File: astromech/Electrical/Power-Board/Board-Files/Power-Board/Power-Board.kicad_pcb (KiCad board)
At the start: 2 copper layers, 119.4 x 96.5 mm, 74 parts, among them J1 BAT_IN_SCREW, J10 HEAD_MOT, J2 BAT_IN_HOLE, J5 E_STOP, J6 CTRL_BRD, J7 JETSON, J8 L_DRIVE, J9 R_DRIVE, Q1 Q_NMOS_DSG, Q2 Q_NMOS_DSG, U1 LTC7003, U2 Logic_Level_Converter, U3 12V_REG, U4 LTC7003, U5 5V_REG, U6 3.3V_REG

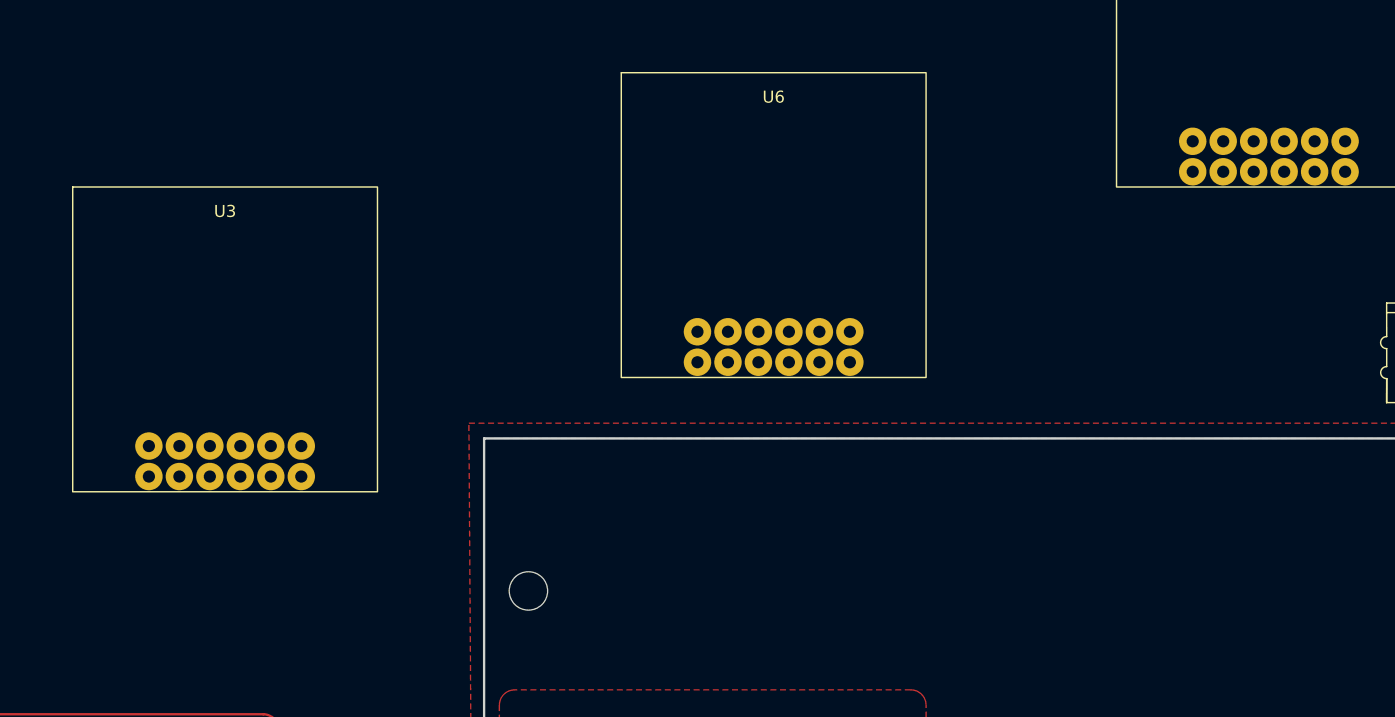
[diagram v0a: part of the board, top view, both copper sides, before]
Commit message: Moved regulator fuses
Moved regulator fuses to voltage input
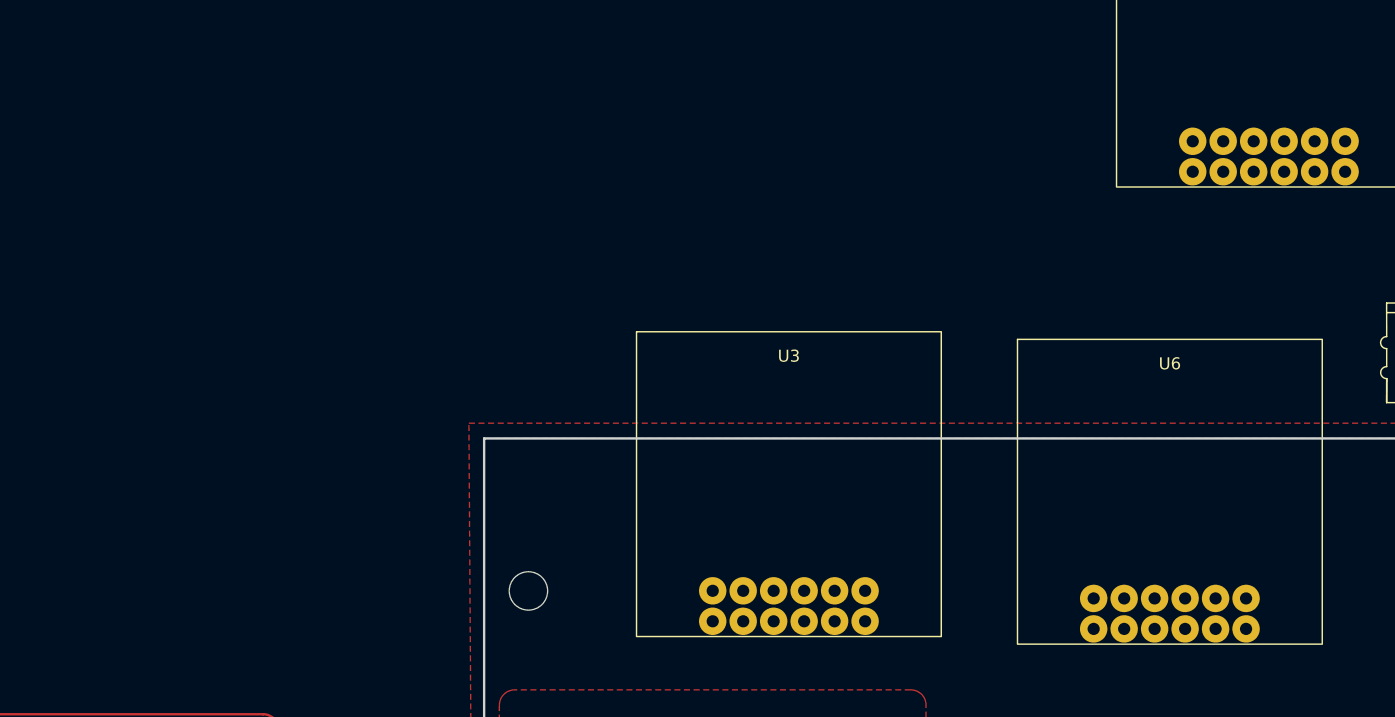
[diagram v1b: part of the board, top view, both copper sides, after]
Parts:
- moved U3 48.5 mm to (101.6, 41.9)
- moved U6 39.8 mm to (133.3, 42.5)
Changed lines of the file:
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@@
   )
   (footprint "astromech-footprints:D36V50Fx" (layer "F.Cu")
-    (at 100.33 20.32)
+    (at 133.35 42.545)
     (property "Sheetfile" "Power-Board.kicad_sch")
     (property "Sheetname" "")
@@
   )
   (footprint "astromech-footprints:D36V50Fx" (layer "F.Cu")
-    (at 54.61 29.845)
-    (property "Sheetfile" "Power-Board.kicad_sch")
-    (property "Sheetname" "")
+    (at 101.6 41.91)
+    (property "Sheetfile" "Power-Board.kicad_sch")
+    (property "Sheetname" "")

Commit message: layout changes
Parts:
- moved SIG-CONV-LV1 389.4 mm to (6.74, 137.1)
- moved SIG-CONV-LV2 382.3 mm to (22.9, 137.4)
- moved C9 245.6 mm to (151.1, 148.0)
- moved 5V4 243.5 mm to (182.2, 123.8)
- moved 5V3 242.2 mm to (170.8, 123.8)
- moved 5V2 241.0 mm to (159.4, 123.8)
- moved SIG-CONV-HV2 240.8 mm to (94.1, 87.6), turned to -90 degrees
- moved 5V1 239.7 mm to (148.0, 123.8)
- moved SIG-CONV-HV1 222.1 mm to (93.9, 108.8), turned to -90 degrees
- moved U3 175.3 mm to (270.5, 88.9), turned to 180 degrees
- moved 3.3V4 148.0 mm to (184.8, 68.6), turned to 90 degrees
- moved U5 133.1 mm to (244.5, 88.9), turned to 180 degrees
- moved 3.3V3 132.8 mm to (184.8, 80.0), turned to 90 degrees
- moved 12V4 127.8 mm to (136.5, 123.8)
- moved 12V3 126.5 mm to (125.1, 123.8)
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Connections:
- F2 pad 1: 12V_REG -> +BATT
- F3 pad 1: 5V_REG -> +BATT
- F4 pad 1: Net-(F4-Pad1) -> Net-(U6-Pad3)
- F4 pad 2: 3.3V_REG -> +BATT
- U3 pad 1: Net-(F2-Pad2) -> 12V_REG
- U3 pad 3: +BATT -> Net-(F2-Pad2)
- U5 pad 1: Net-(F3-Pad2) -> 5V_REG
- U5 pad 3: +BATT -> Net-(F3-Pad2)
- U6 pad 1: Net-(F4-Pad1) -> 3.3V_REG
- U6 pad 3: +BATT -> Net-(U6-Pad3)
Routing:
- removed copper zone on F.Cu, net Net-(F1-Pad1)
- removed copper zone on F.Cu, net POW+

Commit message: First fully routed board version
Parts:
- C1, C10, C2, C3, C4, C5, C6, C7, C8, C9, D1, D2, R1, R10, R11, R12, R13, R14, R2, R3, R4, R5, R6, R7, R8, R9, TP1, TP2, U1, U4: moved to B.Cu
- moved U2 186.1 mm to (159.4, 62.9)
- moved SIG-CONV-LV2 145.6 mm to (138.4, 48.9), turned to 180 degrees
- moved SIG-CONV-LV1 145.5 mm to (122.5, 48.9), turned to 180 degrees
- moved U3 112.3 mm to (158.8, 99.7)
- moved U5 112.3 mm to (132.7, 99.7)
- moved U6 111.6 mm to (106.7, 99.7)
- moved F2 111.1 mm to (158.8, 83.2), turned to 0 degrees
- moved 3.3V4 110.2 mm to (87.0, 119.4), turned to -90 degrees
- moved F3 106.2 mm to (137.8, 83.8), turned to 180 degrees
- moved F4 105.5 mm to (111.8, 83.8), turned to 0 degrees
- moved SIG-CONV-HV1 103.1 mm to (177.8, 48.9), turned to 180 degrees
- moved 3.3V3 101.9 mm to (87.0, 108.6), turned to -90 degrees
- moved D1 100.2 mm to (144.8, 85.7)
- moved 3.3V1 99.1 mm to (87.0, 87.0), turned to -90 degrees
- moved 3.3V2 98.0 mm to (87.0, 97.8), turned to -90 degrees
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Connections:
- SIG-CONV-HV2 pad 3: /ENCA_HV1 -> /ENCA_HV2
- U2 pad 5: /ENCA_HV1 -> /ENCA_HV2
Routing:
- net +BATT: track 0.00 -> 291.7 mm, vias 0 -> 1
- net 12V_REG: track 0.00 -> 231.1 mm
- net POW+: track 0.00 -> 202.6 mm
- net 5V_REG: track 0.00 -> 194.9 mm
- net MOT_VOLTAGE: track 0.00 -> 168.4 mm
- net Net-(J5-Pad2): track 0.00 -> 147.4 mm
- net 3.3V_REG: track 0.00 -> 128.7 mm
- net Net-(Q1-Pad3): track 0.00 -> 100.6 mm, vias 0 -> 1
- net Net-(Q2-Pad3): track 0.00 -> 89.2 mm, vias 0 -> 1
- net Net-(R4-Pad2): track 0.00 -> 84.6 mm, vias 0 -> 2
- net Net-(SIG-CONV-LV1-Pad3): track 0.00 -> 49.6 mm
- net Net-(SIG-CONV-LV1-Pad2): track 0.00 -> 44.3 mm
- net Net-(SIG-CONV-LV2-Pad3): track 0.00 -> 26.1 mm
- net /ENCB_HV1: track 0.00 -> 26.1 mm
- net /ENCA_HV2: track 0.00 -> 24.2 mm
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- added copper zone on F.Cu, net GND
- added copper zone on F.Cu, net Net-(F1-Pad1)
- added copper zone on F.Cu, net POW+

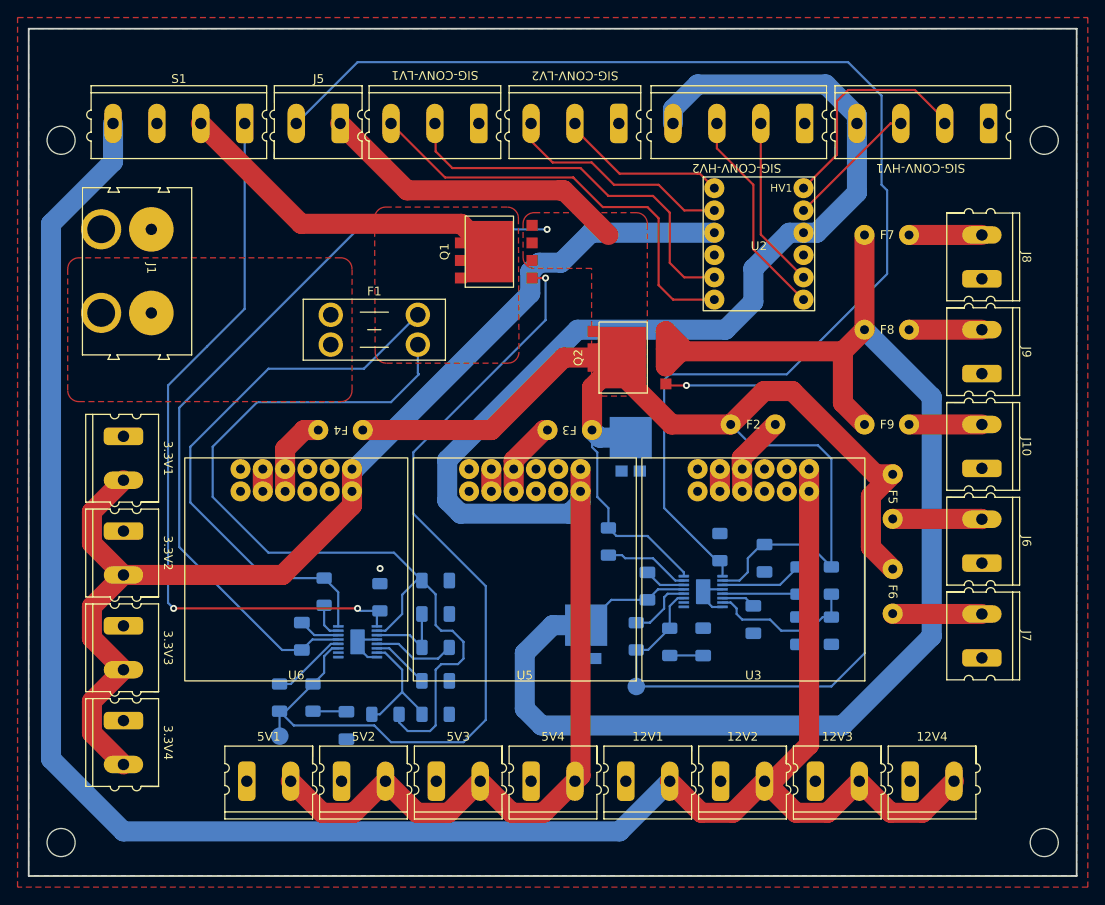
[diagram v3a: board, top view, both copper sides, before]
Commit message: partially updated power board
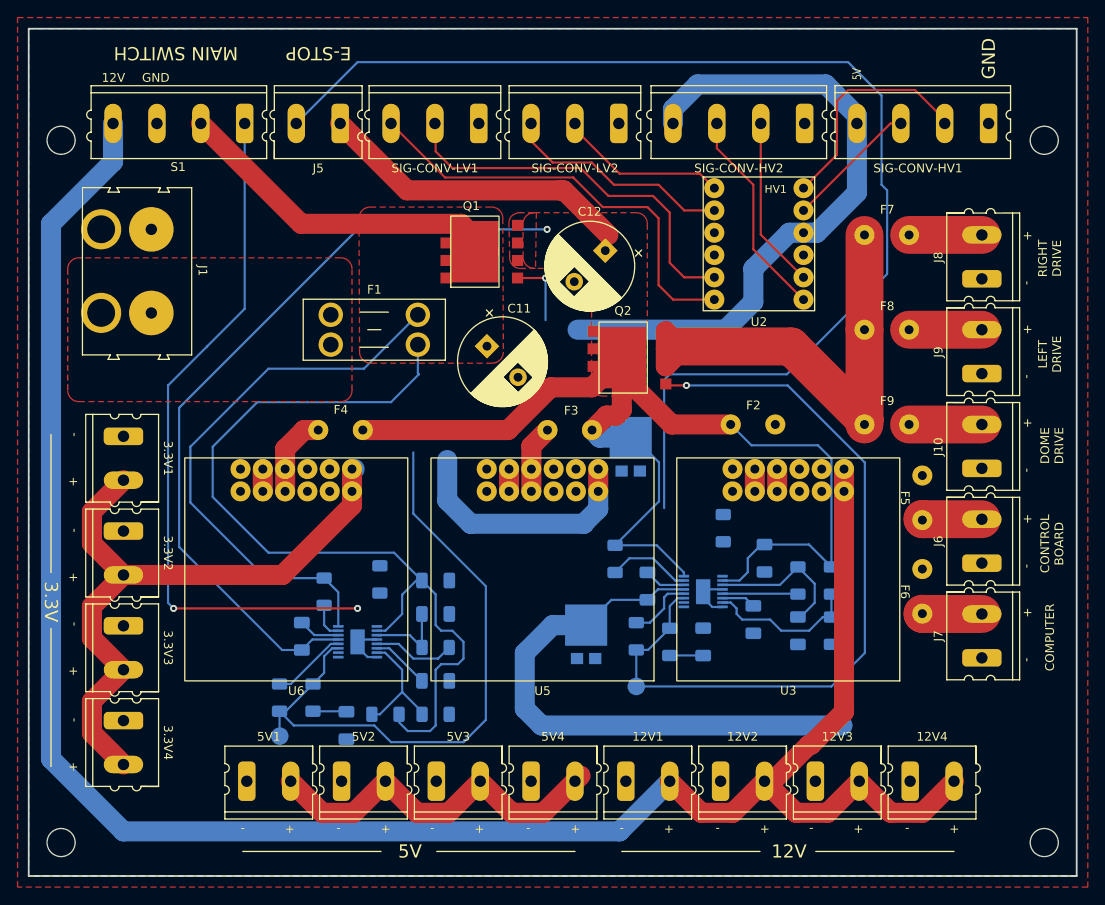
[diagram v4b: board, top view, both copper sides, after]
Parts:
- added C11: 1000 uF, Capacitor_THT:CP_Radial_D10.0mm_P5.00mm, F.Cu at (128.4, 74.3)
- added C12: 1000 uF, Capacitor_THT:CP_Radial_D10.0mm_P5.00mm, F.Cu at (141.9, 63.4)
- moved U3 3.98 mm to (162.7, 99.7)
- moved F5 3.38 mm to (178.0, 91.6)
- moved F6 3.38 mm to (178.0, 102.2)
- moved R10 2.19 mm to (155.3, 95.0)
- moved R11 2.12 mm to (143.0, 98.5)
- moved R4 2.03 mm to (116.2, 100.8)
- moved U5 2.01 mm to (134.7, 99.7)
- moved Q1 1.65 mm to (127.9, 63.5)
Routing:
- net 3.3V_REG: track 128.7 -> 75.1 mm
- net 5V_REG: track 194.9 -> 144.7 mm
- net MOT_VOLTAGE: track 168.4 -> 119.8 mm
- net +BATT: track 291.7 -> 258.0 mm
- net Net-(Q1-Pad3): track 100.6 -> 80.9 mm
- net Net-(J5-Pad2): track 147.4 -> 136.7 mm
- net Net-(F2-Pad2): track 9.31 -> 2.54 mm
- net Net-(R4-Pad2): track 84.6 -> 80.1 mm
- net Net-(F6-Pad2): track 10.2 -> 6.80 mm
- net Net-(F5-Pad2): track 10.2 -> 6.86 mm
- net 12V_REG: track 231.1 -> 232.9 mm
- net Net-(F3-Pad2): track 8.86 -> 7.75 mm
- net GND: vias 1 -> 0
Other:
- board text added: "+"
- board text added: "-"
- board text added: "12V"
- board text added: "3.3V"
- board text added: "5V"
- board text added: "COMPUTER"
- board text added: "CONTROL BOARD"
- board text added: "DOME DRIVE"
- board text added: "E-STOP"
- board text added: "GND"
- board text added: "LEFT DRIVE"
- board text added: "MAIN SWITCH"
- board text added: "RIGHT DRIVE"

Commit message: revA done
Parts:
- added ?: , , F.Cu at (133.3, 69.0)
- added ?: , , F.Cu at (116.2, 78.7)
- added G***: LOGO, LOGO, F.Cu at (118.3, 61.5)
- D1, D2: moved to F.Cu
- moved D2 55.2 mm to (174.6, 64.3), turned to -90 degrees
- moved J2 13.8 mm to (98.3, 65.1)
- moved F7 5.64 mm to (176.7, 56.6)
- moved F9 4.29 mm to (173.9, 78.9)
- moved D1 4.01 mm to (148.7, 86.3), turned to 180 degrees
- moved R11 3.06 mm to (145.3, 96.5)
- moved C8 1.45 mm to (145.3, 101.9)
- moved J1 0.78 mm to (90.5, 64.7)
- renumbered SIG-CONV-HV1 to ENCODER-HV1, SIG-CONV-HV2 to ENCODER-HV2, SIG-CONV-LV1 to ENCODER-LV1, SIG-CONV-LV2 to ENCODER-LV2
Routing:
- net 5V_REG: track 144.7 -> 205.4 mm
- net 3.3V_REG: track 75.1 -> 131.6 mm
- net +BATT: track 258.0 -> 297.7 mm, vias 1 -> 2
- net MOT_VOLTAGE: track 119.8 -> 94.0 mm, vias 0 -> 1
- net Net-(Q1-Pad3): track 80.9 -> 101.6 mm
- net Net-(J5-Pad2): track 136.7 -> 145.9 mm
- net Net-(R4-Pad2): track 80.1 -> 86.9 mm
- net Net-(F2-Pad2): track 2.54 -> 7.71 mm
- net Net-(R11-Pad1): track 9.56 -> 6.73 mm
- net Net-(Q2-Pad3): track 89.2 -> 92.0 mm
- net Net-(F9-Pad2): track 8.29 -> 10.2 mm
- net Net-(C8-Pad1): track 4.74 -> 6.07 mm
- net Net-(F7-Pad2): track 8.29 -> 7.65 mm
- net GND: vias 0 -> 2
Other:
- board text added: "1"
- board text added: "1/28/2023"
- board text added: "2"
- board text added: "3"
- board text added: "4"
- board text added: "Astromech Power Board"
- board text added: "BATTERY IN"
- board text added: "CAP-BYPASS"
- board text added: "ENCODER-HV1"
- board text added: "ENCODER-HV2"
- board text added: "ENCODER-LV1"
- board text added: "ENCODER-LV2"
- board text added: "Ethan Robin"
- board text added: "Rev A.1"

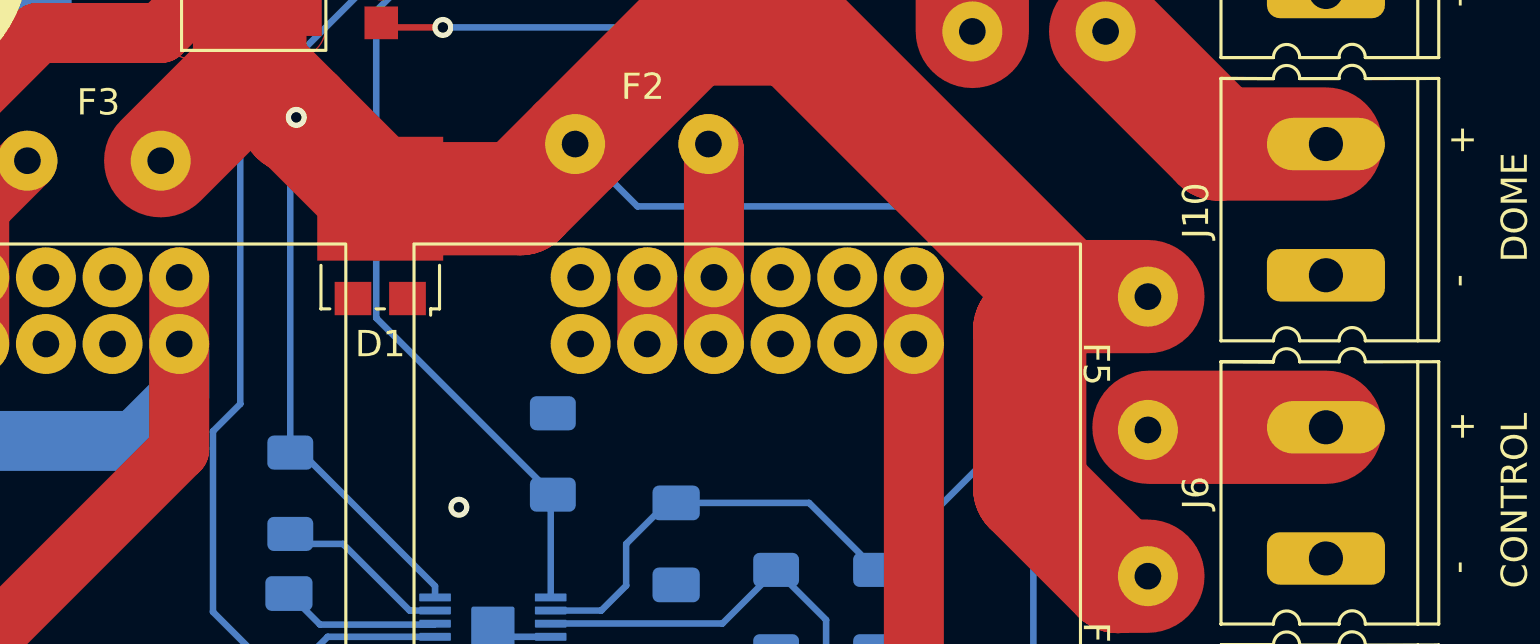
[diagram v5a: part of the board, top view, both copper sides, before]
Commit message: board wire bits removed
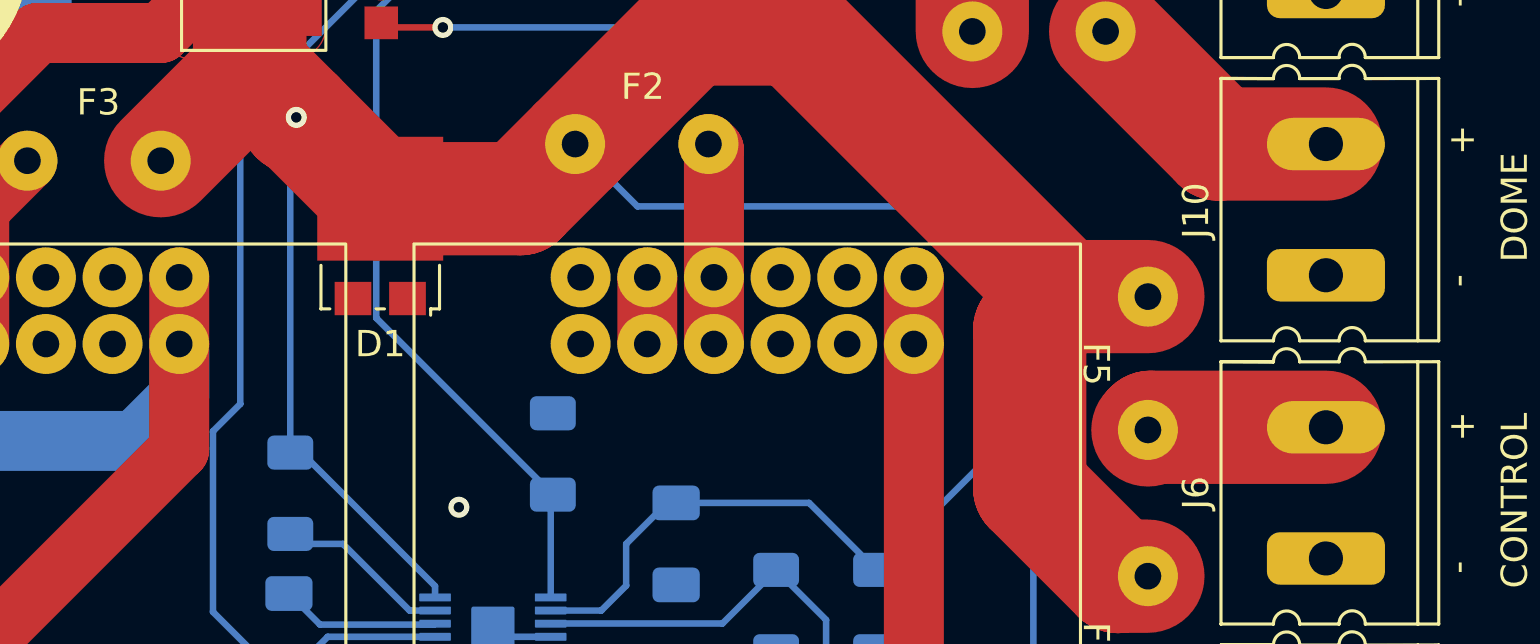
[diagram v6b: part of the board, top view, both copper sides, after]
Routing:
- net +BATT: track 297.7 -> 296.9 mm
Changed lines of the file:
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@@
   (segment (start 158.115 98.425) (end 159.6775 96.8625) (width 0.25) (layer "B.Cu") (net 9))
   (segment (start 165.0875 96.8625) (end 167.64 99.415) (width 0.25) (layer "B.Cu") (net 9))
-  (segment (start 140.97 84.415) (end 140.375 83.82) (width 0.25) (layer "B.Cu") (net 9))
   (segment (start 93.345 97.155) (end 105.0675 108.8775) (width 0.25) (layer "B.Cu") (net 9))
   (segment (start 150.83155 100.03155) (end 145.7446 94.9446) (width 0.25) (layer "B.Cu") (net 9))
@@
   (segment (start 172.2374 67.7926) (end 172.2374 44.6024) (width 0.25) (layer "B.Cu") (net 15))
   (segment (start 149.225 77.47) (end 162.56 77.47) (width 0.25) (layer "B.Cu") (net 15))
-  (segment (start 184.745 93.94) (end 184.785 93.98) (width 2.286) (layer "F.Cu") (net 16))
-  (segment (start 184.785 93.98) (end 178.04 93.98) (width 4.318) (layer "F.Cu") (net 16))
+  (segment (start 178.1 93.98) (end 178 94.08) (width 4.318) (layer "F.Cu") (net 16))
+  (segment (start 184.785 93.98) (end 178.1 93.98) (width 4.318) (layer "F.Cu") (net 16))
   (segment (start 178.04 104.775) (end 178 104.735) (width 4.318) (layer "F.Cu") (net 17))
   (segment (start 184.785 104.775) (end 178.04 104.775) (width 4.318) (layer "F.Cu") (net 17))
